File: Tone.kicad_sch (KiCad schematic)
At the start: 9 parts, among them U10 74LS273, U13 74LS273, U16 74LS541, U19 74LS541, U22 4040, U25 74LS85, U28 74LS85, U31 74LS85, U65 74LS00

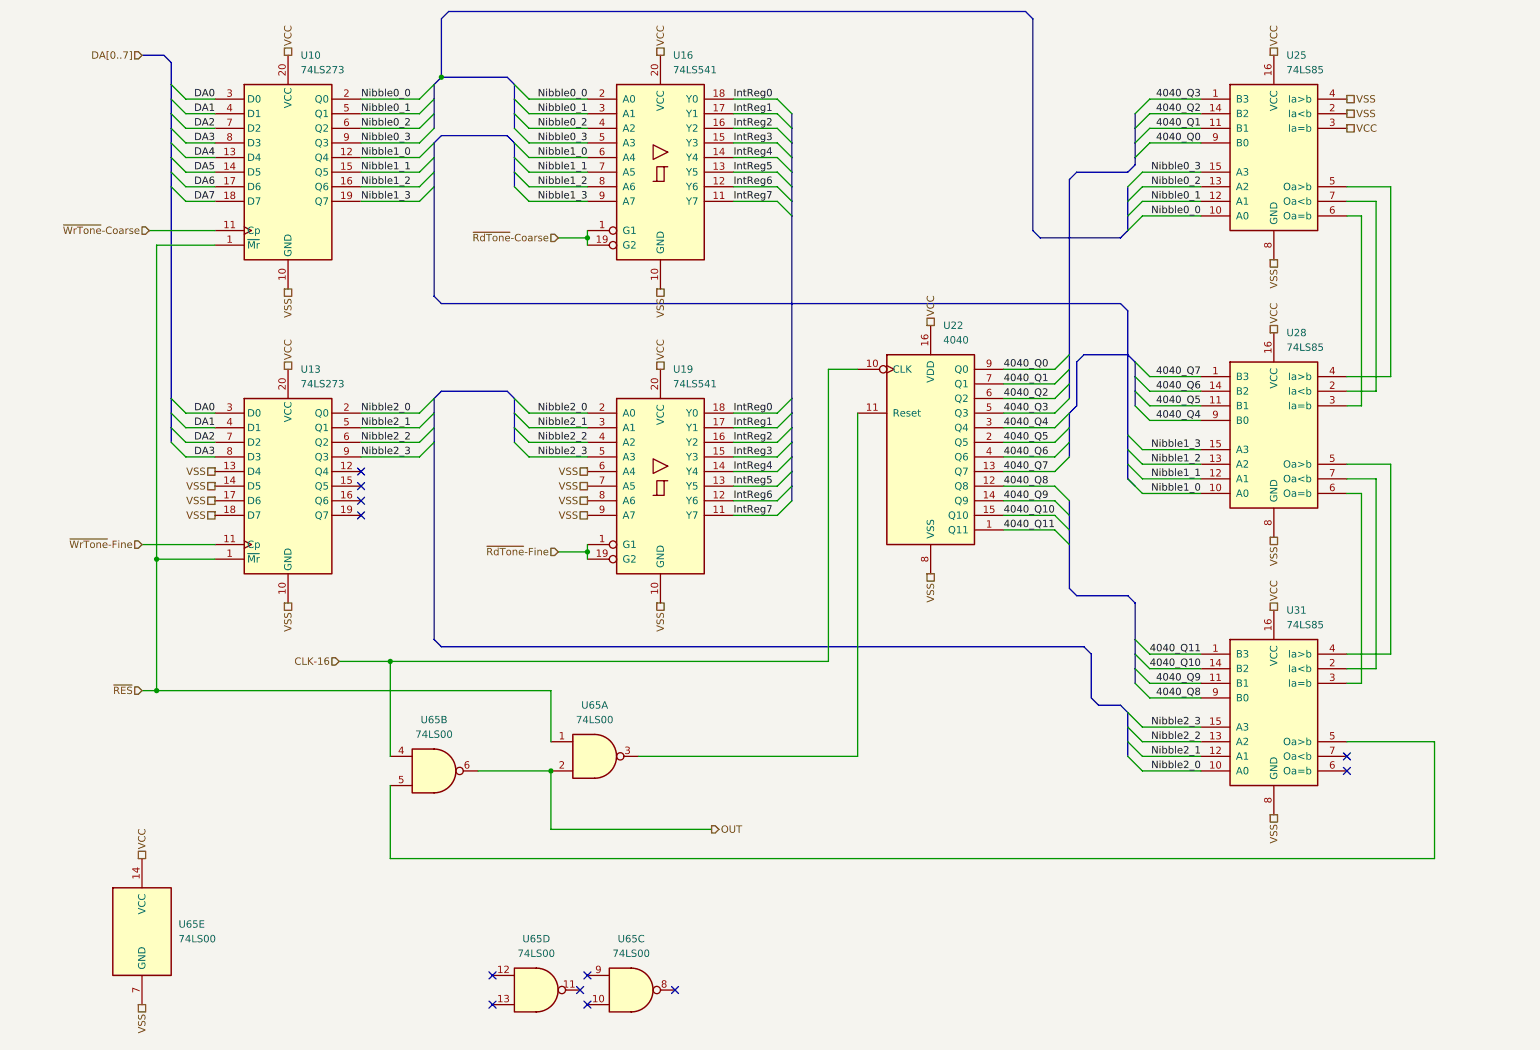
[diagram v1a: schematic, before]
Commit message: Correction sous-page Tone.kicad_sch
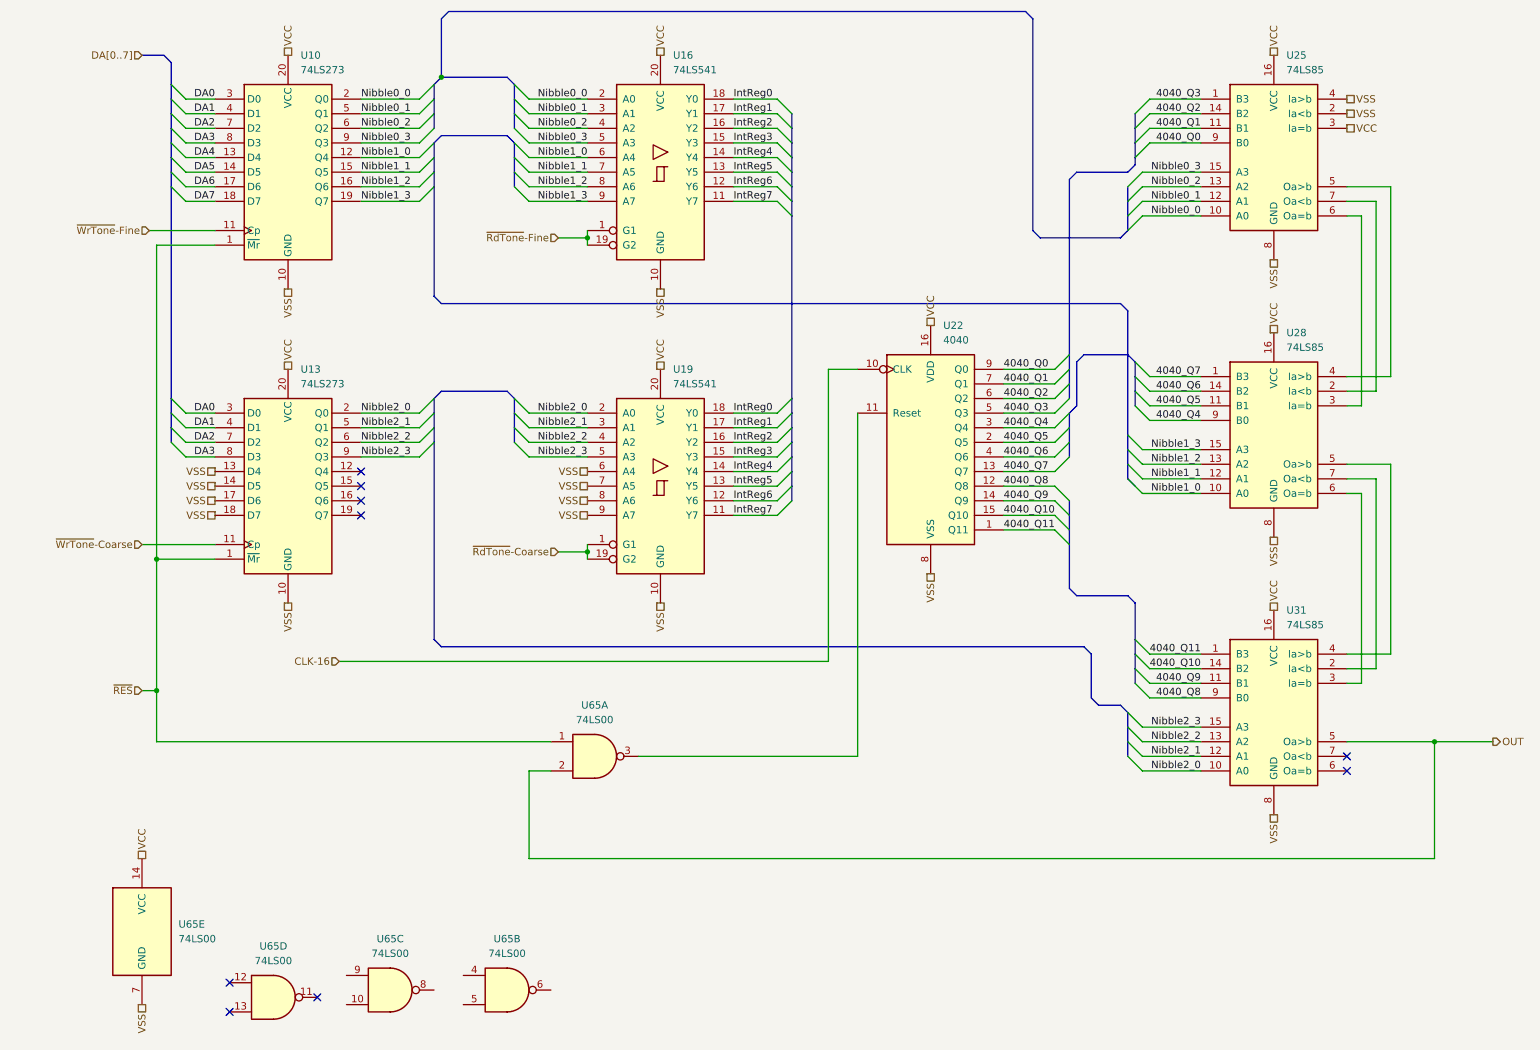
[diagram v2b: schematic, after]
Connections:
- net CLK-16: no longer U65.4
- net OUT: now also U31.5 (Oa>b); no longer U65.6
- net ~{RdTone}-Coarse: now also U19.1 (G1), U19.19 (G2); no longer U16.1 (G1), U16.19 (G2)
- net ~{RdTone}-Fine: now also U16.1 (G1), U16.19 (G2); no longer U19.1 (G1), U19.19 (G2)
- net ~{WrTone}-Coarse: now also U13.11 (Cp); no longer U10.11 (Cp)
- net ~{WrTone}-Fine: now also U10.11 (Cp); no longer U13.11 (Cp)
- net at U65.5: no longer U31.5 (Oa>b)
- no-connect marks 12 -> 9
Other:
- moved on the sheet: U65B, U65C, U65D
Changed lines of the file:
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@@
 	(paper "A4")
 	(junction
-		(at 102.87 147.32)
-		(diameter 0)
-		(color 0 0 0 0)
-	)
-	(junction
 		(at 83.82 26.67)
 		(diameter 0)
@@
 	)
 	(junction
-		(at 74.93 128.27)
+		(at 109.22 109.22)
 		(diameter 0)
 		(color 0 0 0 0)
 	)
 	(junction
-		(at 109.22 109.22)
+		(at 109.22 54.61)
 		(diameter 0)
 		(color 0 0 0 0)
 	)
 	(junction
-		(at 109.22 54.61)
+		(at 256.54 142.24)
 		(diameter 0)
 		(color 0 0 0 0)
@@
 	)
 	(no_connect
-		(at 92.71 182.88)
+		(at 46.99 184.15)
 	)
 	(no_connect
@@
 	)
 	(no_connect
-		(at 107.95 185.42)
+		(at 62.23 186.69)
 	)
 	(no_connect
@@
 	)
 	(no_connect
-		(at 109.22 182.88)
-	)
-	(no_connect
-		(at 109.22 187.96)
-	)
-	(no_connect
-		(at 92.71 187.96)
-	)
-	(no_connect
-		(at 124.46 185.42)
+		(at 46.99 189.23)
 	)
 	(no_connect
@@
 	(wire
 		(pts
-			(xy 34.29 133.35) (xy 102.87 133.35)
+			(xy 34.29 142.24) (xy 102.87 142.24)
 		)
 		(stroke
@@
 		)
 	)
+	(wire
+		(pts
+			(xy 256.54 142.24) (xy 266.7 142.24)
+		)
+		(stroke
+			(width 0)
+			(type default)
+		)
+	)
 	(bus
 		(pts
@@
 		)
 	)
-	(wire
-		(pts
-			(xy 74.93 162.56) (xy 74.93 149.86)
-		)
-		(stroke
-			(width 0)
-			(type default)
-		)
-	)
 	(bus
 		(pts
@@
 		)
 	)
-	(wire
-		(pts
-			(xy 102.87 147.32) (xy 102.87 157.48)
-		)
-		(stroke
-			(width 0)
-			(type default)
-		)
-	)
 	(bus
 		(pts
@@
 	(wire
 		(pts
-			(xy 74.93 162.56) (xy 256.54 162.56)
+			(xy 243.84 83.82) (xy 241.3 83.82)
 		)
 		(stroke
@@
 	(wire
 		(pts
-			(xy 243.84 83.82) (xy 241.3 83.82)
+			(xy 99.06 162.56) (xy 256.54 162.56)
+		)
+		(stroke
+			(width 0)
+			(type default)
+		)
+	)
+	(wire
+		(pts
+			(xy 99.06 147.32) (xy 102.87 147.32)
 		)
 		(stroke
@@
 	(wire
 		(pts
+			(xy 99.06 147.32) (xy 99.06 162.56)
+		)
+		(stroke
+			(width 0)
+			(type default)
+		)
+	)
+	(wire
+		(pts
 			(xy 134.62 97.79) (xy 142.24 97.79)
 		)
@@
 		)
 	)
-	(wire
-		(pts
-			(xy 90.17 147.32) (xy 102.87 147.32)
-		)
-		(stroke
-			(width 0)
-			(type default)
-		)
-	)
 	(bus
 		(pts
@@
 		)
 	)
-	(wire
-		(pts
-			(xy 74.93 128.27) (xy 151.13 128.27)
-		)
-		(stroke
-			(width 0)
-			(type default)
-		)
-	)
 	(bus
 		(pts
@@
 		)
 	)
-	(wire
-		(pts
-			(xy 102.87 157.48) (xy 130.81 157.48)
-		)
-		(stroke
-			(width 0)
-			(type default)
-		)
-	)
 	(bus
 		(pts
@@
 	(wire
 		(pts
-			(xy 66.04 128.27) (xy 74.93 128.27)
+			(xy 66.04 128.27) (xy 151.13 128.27)
 		)
 		(stroke
@@
 	(wire
 		(pts
-			(xy 102.87 133.35) (xy 102.87 142.24)
+			(xy 34.29 133.35) (xy 34.29 142.24)
 		)
 		(stroke
@@
 		)
 	)
-	(wire
-		(pts
-			(xy 74.93 128.27) (xy 74.93 144.78)
-		)
-		(stroke
-			(width 0)
-			(type default)
-		)
-	)
 	(bus
 		(pts
@@
 	(hierarchical_label "OUT"
 		(shape output)
-		(at 130.81 157.48 0)
+		(at 266.7 142.24 0)
 		(effects
 			(font
@@
 	(hierarchical_label "~{RdTone}-Fine"
 		(shape input)
-		(at 104.14 109.22 180)
+		(at 104.14 54.61 180)
 		(effects
 			(font
@@
 	(hierarchical_label "~{WrTone}-Coarse"
 		(shape input)
-		(at 33.02 53.34 180)
+		(at 31.75 107.95 180)
 		(effects
 			(font
@@
 	(hierarchical_label "~{RdTone}-Coarse"
 		(shape input)
-		(at 104.14 54.61 180)
+		(at 104.14 109.22 180)
 		(effects
 			(font
@@
 	(hierarchical_label "~{WrTone}-Fine"
 		(shape input)
-		(at 31.75 107.95 180)
+		(at 33.02 53.34 180)
 		(effects
 			(font
@@
 	(symbol
 		(lib_id "74xx:74LS00")
-		(at 116.84 185.42 0)
+		(at 74.93 185.42 0)
 		(unit 3)
 		(exclude_from_sim no)
@@
 		(fields_autoplaced yes)
 		(property "Reference" "U65"
-			(at 116.8317 176.53 0)
+			(at 74.9217 176.53 0)
 			(effects
 				(font
@@
 		)
 		(property "Value" "74LS00"
-			(at 116.8317 179.07 0)
+			(at 74.9217 179.07 0)
 			(effects
 				(font
@@
 		)
 		(property "Footprint" ""
-			(at 116.84 185.42 0)
+			(at 74.93 185.42 0)
 			(effects
 				(font
@@
 		)
 		(property "Datasheet" "http://www.ti.com/lit/gpn/sn74ls00"
-			(at 116.84 185.42 0)
+			(at 74.93 185.42 0)
 			(effects
 				(font
@@
 		)
 		(property "Description" ""
-			(at 116.84 185.42 0)
+			(at 74.93 185.42 0)
 			(effects
 				(font
@@
 	(symbol
 		(lib_id "74xx:74LS00")
-		(at 82.55 147.32 0)
+		(at 95.25 185.42 0)
 		(unit 2)
 		(exclude_from_sim no)
@@
 		(fields_autoplaced yes)
 		(property "Reference" "U65"
-			(at 82.5417 138.43 0)
+			(at 95.2417 176.53 0)
 			(effects
 				(font
@@
 		)
 		(property "Value" "74LS00"
-			(at 82.5417 140.97 0)
+			(at 95.2417 179.07 0)
 			(effects
 				(font
@@
 		)
 		(property "Footprint" ""
-			(at 82.55 147.32 0)
+			(at 95.25 185.42 0)
 			(effects
 				(font
@@
 		)
 		(property "Datasheet" "http://www.ti.com/lit/gpn/sn74ls00"
-			(at 82.55 147.32 0)
+			(at 95.25 185.42 0)
 			(effects
 				(font
@@
 		)
 		(property "Description" ""
-			(at 82.55 147.32 0)
+			(at 95.25 185.42 0)
 			(effects
 				(font
@@
 	(symbol
 		(lib_id "74xx:74LS00")
-		(at 100.33 185.42 0)
+		(at 54.61 186.69 0)
 		(unit 4)
 		(exclude_from_sim no)
@@
 		(fields_autoplaced yes)
 		(property "Reference" "U65"
-			(at 100.3217 176.53 0)
+			(at 54.6017 177.8 0)
 			(effects
 				(font
@@
 		)
 		(property "Value" "74LS00"
-			(at 100.3217 179.07 0)
+			(at 54.6017 180.34 0)
 			(effects
 				(font
@@
 		)
 		(property "Footprint" ""
-			(at 100.33 185.42 0)
+			(at 54.61 186.69 0)
 			(effects
 				(font
@@
 		)
 		(property "Datasheet" "http://www.ti.com/lit/gpn/sn74ls00"
-			(at 100.33 185.42 0)
+			(at 54.61 186.69 0)
 			(effects
 				(font
@@
 		)
 		(property "Description" ""
-			(at 100.33 185.42 0)
+			(at 54.61 186.69 0)
 			(effects
 				(font
